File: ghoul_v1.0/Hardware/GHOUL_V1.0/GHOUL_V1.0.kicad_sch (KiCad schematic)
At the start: 38 parts, among them J1 XT30, J2 Conn_01x02, J3 Conn_01x02, M2 Motor_Servo, U1 LM1084-ADJ, U2 DS18S20, U3 Xbee, U4 TPS62133, U5 MS5607-02BA, U6 SAM-M8Q, U7 Teensy4.1

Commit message: shuffling things around
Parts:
- U7: footprint teensy.pretty-master:Teensy41 -> BPP_Lib:Teensy4_1
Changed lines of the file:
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@@
 	(wire
 		(pts
+			(xy 142.24 62.23) (xy 142.24 60.96)
+		)
+		(stroke
+			(width 0)
+			(type default)
+		)
+	)
+	(wire
+		(pts
 			(xy 57.15 62.23) (xy 57.15 63.5)
 		)
@@
 			)
 		)
-		(property "Footprint" "teensy.pretty-master:Teensy41"
+		(property "Footprint" "BPP_Lib:Teensy4_1"
 			(at 90.932 128.016 0)
 			(effects
@@
 		(lib_name "GND_1")
 		(lib_id "power:GND")
-		(at 142.24 60.96 0)
+		(at 142.24 62.23 0)
 		(unit 1)
 		(exclude_from_sim no)
@@
 		(on_board yes)
 		(dnp no)
-		(fields_autoplaced yes)
 		(property "Reference" "#PWR01"
-			(at 142.24 67.31 0)
+			(at 142.24 68.58 0)
 			(effects
 				(font
@@
 		)
 		(property "Footprint" ""
-			(at 142.24 60.96 0)
+			(at 142.24 62.23 0)
 			(effects
 				(font
@@
 		)
 		(property "Datasheet" ""
-			(at 142.24 60.96 0)
+			(at 142.24 62.23 0)
 			(effects
 				(font
@@
 		)
 		(property "Description" ""
-			(at 142.24 60.96 0)
+			(at 142.24 62.23 0)
 			(effects
 				(font

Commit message: almost have V1.0 cleaned up
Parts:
- BT2: footprint ML414H_IV01E:SEIKO_ML414H_IV01E -> BPP_Lib:SEIKO_ML414H_IV01E
- C5, C7, C8: footprint Capacitor_SMD:C_0201_0603Metric_Pad0.64x0.40mm_HandSolder -> Capacitor_SMD:C_0603_1608Metric_Pad1.08x0.95mm_HandSolder
- J2, J3: footprint (none) -> Connector_JST:JST_EH_B2B-EH-A_1x02_P2.50mm_Vertical
- R10, R6, R7: footprint Resistor_SMD:R_0201_0603Metric_Pad0.64x0.40mm_HandSolder -> Resistor_SMD:R_0603_1608Metric_Pad0.98x0.95mm_HandSolder
- U1: footprint (none) -> Package_TO_SOT_SMD:TO-263-3_TabPin2
- U3: footprint GHOULFootPrints:XBee Explorer -> BPP_Lib:XBee Explorer
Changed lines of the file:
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@@
 			)
 		)
-		(property "Footprint" "Capacitor_SMD:C_0201_0603Metric_Pad0.64x0.40mm_HandSolder"
+		(property "Footprint" "Capacitor_SMD:C_0603_1608Metric_Pad1.08x0.95mm_HandSolder"
 			(at 241.3 92.71 0)
 			(effects
@@
 			)
 		)
-		(property "Footprint" "Resistor_SMD:R_0201_0603Metric_Pad0.64x0.40mm_HandSolder"
+		(property "Footprint" "Resistor_SMD:R_0603_1608Metric_Pad0.98x0.95mm_HandSolder"
 			(at 257.81 82.55 0)
 			(effects
@@
 			)
 		)
-		(property "Footprint" "GHOULFootPrints:XBee Explorer"
+		(property "Footprint" "BPP_Lib:XBee Explorer"
 			(at 119.634 147.828 0)
 			(effects
@@
 			)
 		)
-		(property "Footprint" "ML414H_IV01E:SEIKO_ML414H_IV01E"
+		(property "Footprint" "BPP_Lib:SEIKO_ML414H_IV01E"
 			(at 269.24 91.186 90)
 			(effects
@@
 			)
 		)
-		(property "Footprint" "Resistor_SMD:R_0201_0603Metric_Pad0.64x0.40mm_HandSolder"
+		(property "Footprint" "Resistor_SMD:R_0603_1608Metric_Pad0.98x0.95mm_HandSolder"
 			(at 273.05 106.68 0)
 			(effects
@@
 			)
 		)
-		(property "Footprint" "Resistor_SMD:R_0201_0603Metric_Pad0.64x0.40mm_HandSolder"
+		(property "Footprint" "Resistor_SMD:R_0603_1608Metric_Pad0.98x0.95mm_HandSolder"
 			(at 273.05 104.14 0)
 			(effects
@@
 			)
 		)
-		(property "Footprint" ""
+		(property "Footprint" "Connector_JST:JST_EH_B2B-EH-A_1x02_P2.50mm_Vertical"
 			(at 226.06 73.66 0)
 			(effects
@@
 			)
 		)
-		(property "Footprint" "Capacitor_SMD:C_0201_0603Metric_Pad0.64x0.40mm_HandSolder"
+		(property "Footprint" "Capacitor_SMD:C_0603_1608Metric_Pad1.08x0.95mm_HandSolder"
 			(at 245.11 92.71 0)
 			(effects
@@
 			)
 		)
-		(property "Footprint" ""
+		(property "Footprint" "Connector_JST:JST_EH_B2B-EH-A_1x02_P2.50mm_Vertical"
 			(at 209.55 81.28 0)
 			(effects
@@
 			)
 		)
-		(property "Footprint" ""
+		(property "Footprint" "Package_TO_SOT_SMD:TO-263-3_TabPin2"
 			(at 173.99 67.31 0)
 			(effects
@@
 			)
 		)
-		(property "Footprint" "Capacitor_SMD:C_0201_0603Metric_Pad0.64x0.40mm_HandSolder"
+		(property "Footprint" "Capacitor_SMD:C_0603_1608Metric_Pad1.08x0.95mm_HandSolder"
 			(at 278.13 91.44 0)
 			(effects

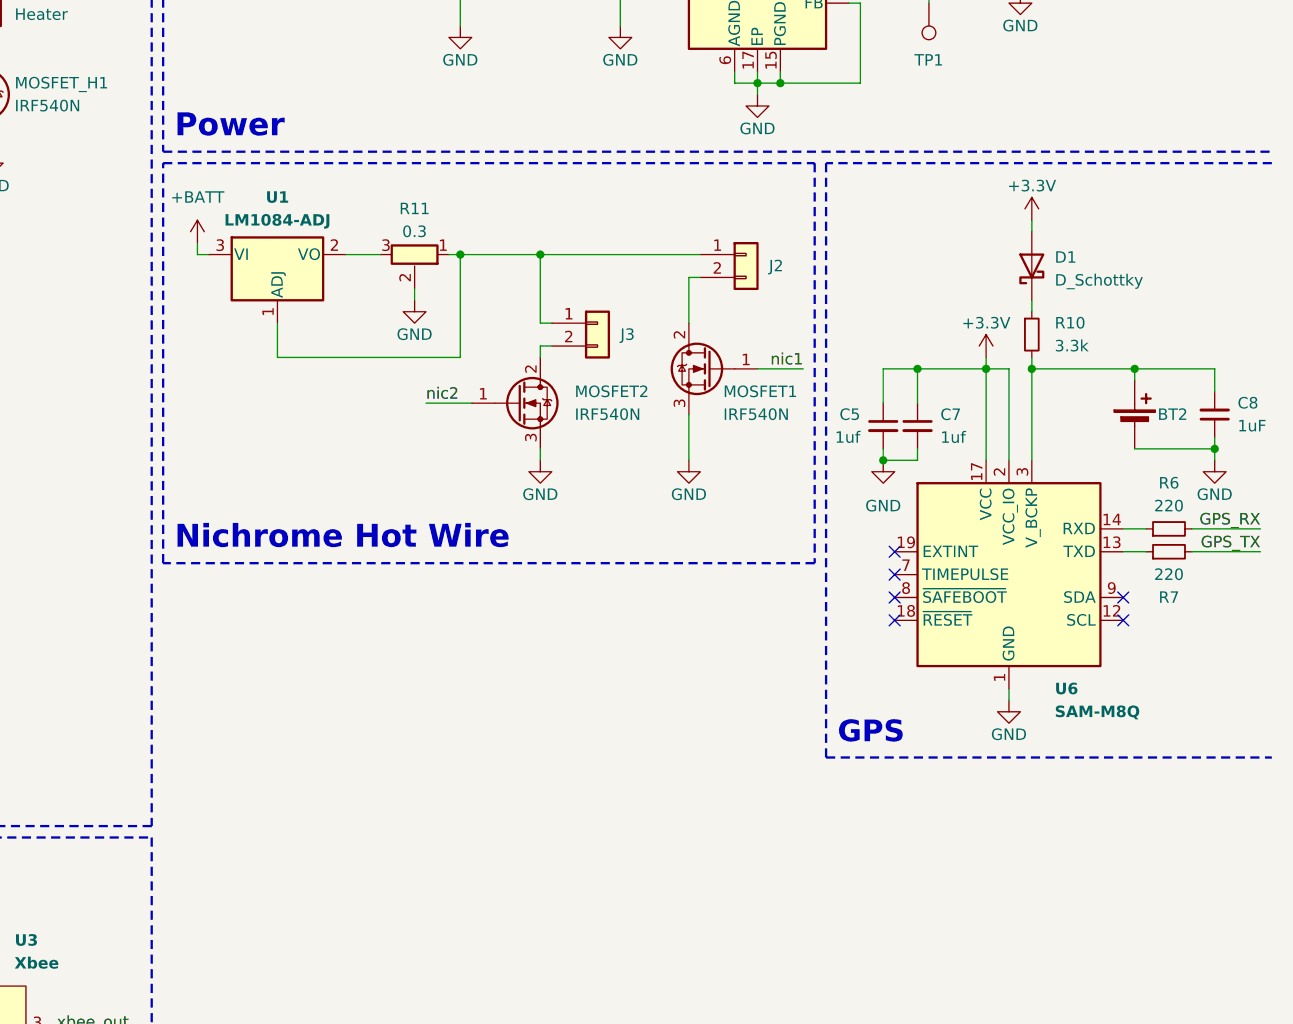
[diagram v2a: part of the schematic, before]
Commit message: switched GPS received, added via stitching, axial R to SMD
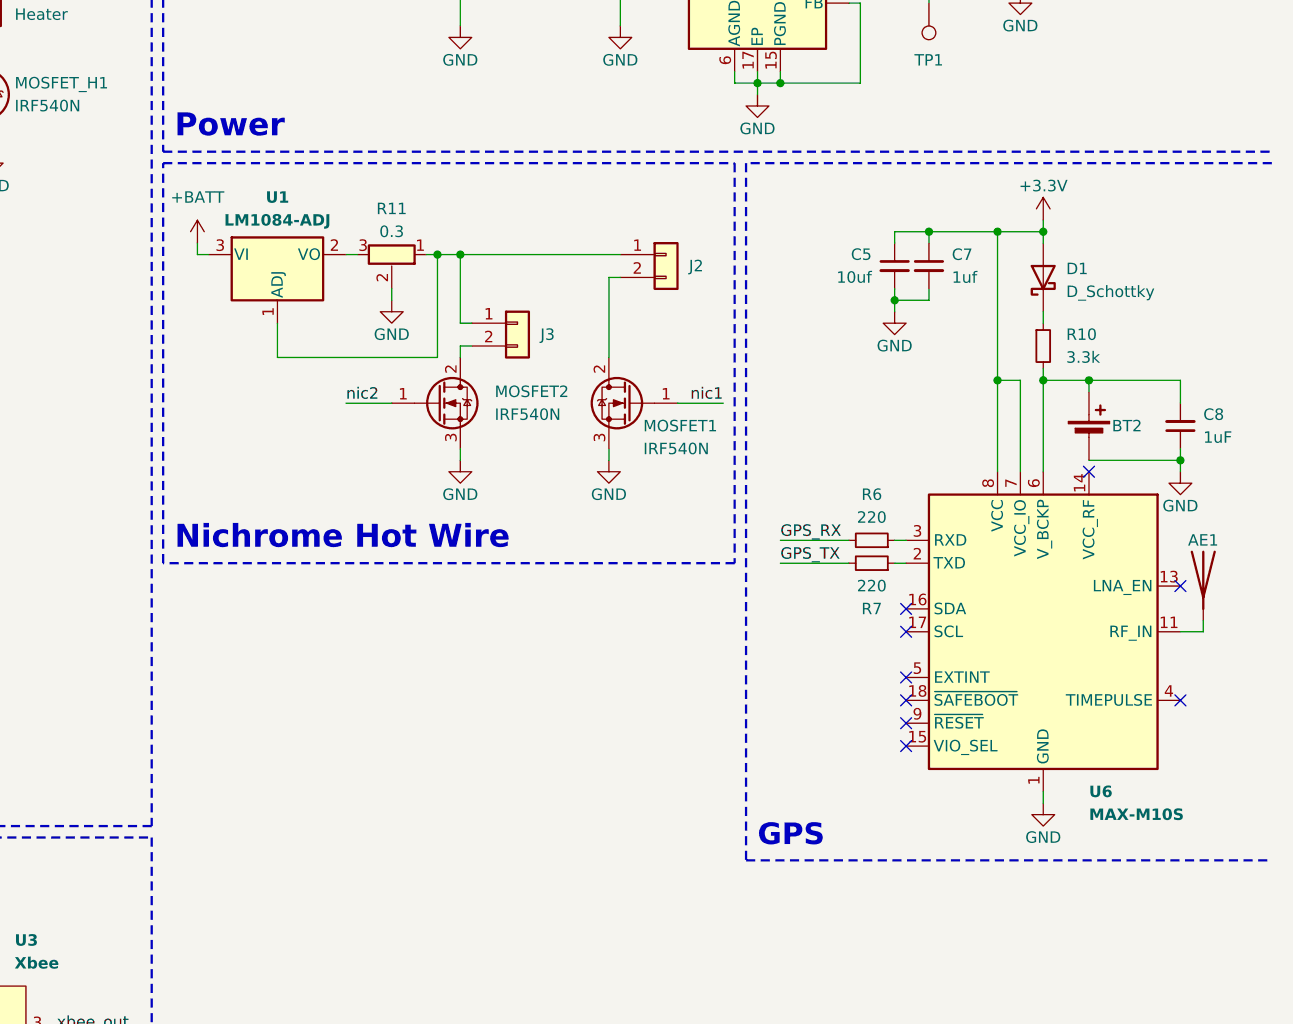
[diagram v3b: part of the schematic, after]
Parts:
- removed U6: SAM-M8Q, RF_GPS:ublox_SAM-M8Q, symbol RF_GPS:SAM-M8Q
- added AE1: 1575AT43A0040001E, BPP_Lib:ANT_1575AT_JOT-M, symbol Device:Antenna
- added U6: MAX-M10S, RF_GPS:ublox_MAX, symbol RF_GPS:MAX-M10S
- C5: value 1uf -> 10uf
- L1: footprint Inductor_SMD:L_Coilcraft_XxL4040 -> Inductor_SMD:L_Vishay_IHLP-1212
- R2, R3, R4: footprint Resistor_THT:R_Axial_DIN0204_L3.6mm_D1.6mm_P7.62mm_Horizontal -> Resistor_SMD:R_0603_1608Metric
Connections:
- net +3.3V: now also U6.7 (VCC_IO), U6.8 (VCC)
- net GND: now also U6.1 (GND), U6.10 (GND), U6.12 (GND)
- net at BT2.1 (+), C8.2, R10.2: now also U6.6 (V_BCKP)
- net at R7.1: now also U6.2 (TXD)
- net at R6.1: now also U6.3 (RXD)
- new net: AE1.1 (A), U6.11 (RF_IN)
- no-connect marks 52 -> 55
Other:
- moved on the sheet: BT2, C5, C7, C8, D1, J2, J3, MOSFET1, MOSFET2, R10, R11, R6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
